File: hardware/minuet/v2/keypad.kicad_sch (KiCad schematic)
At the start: 3 parts, among them J501 G800LE300018YEU, J502 MTJ-889X1, J503 MTJ-669X1

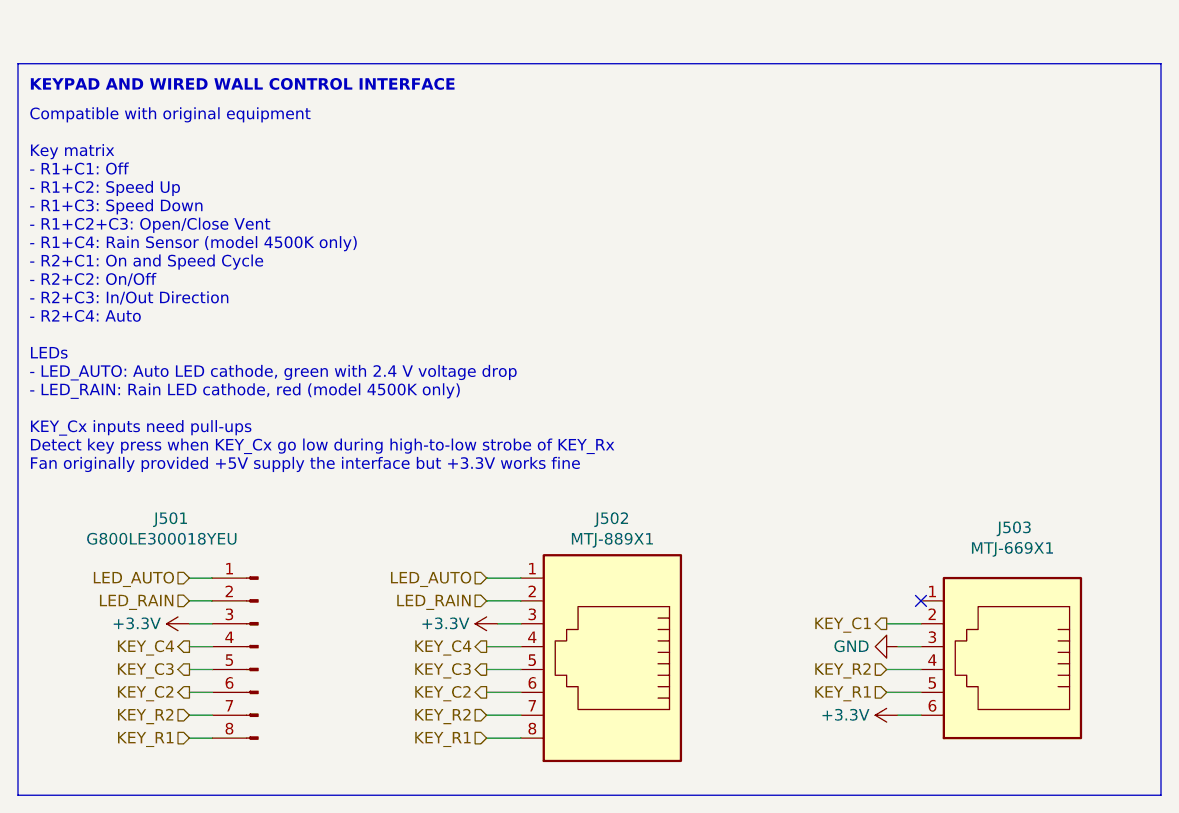
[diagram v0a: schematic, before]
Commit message: Finalize Minuet v2.1 for manufacture.
This revision uses a different motor controller and buck converter
and remedies errata from v2.0.
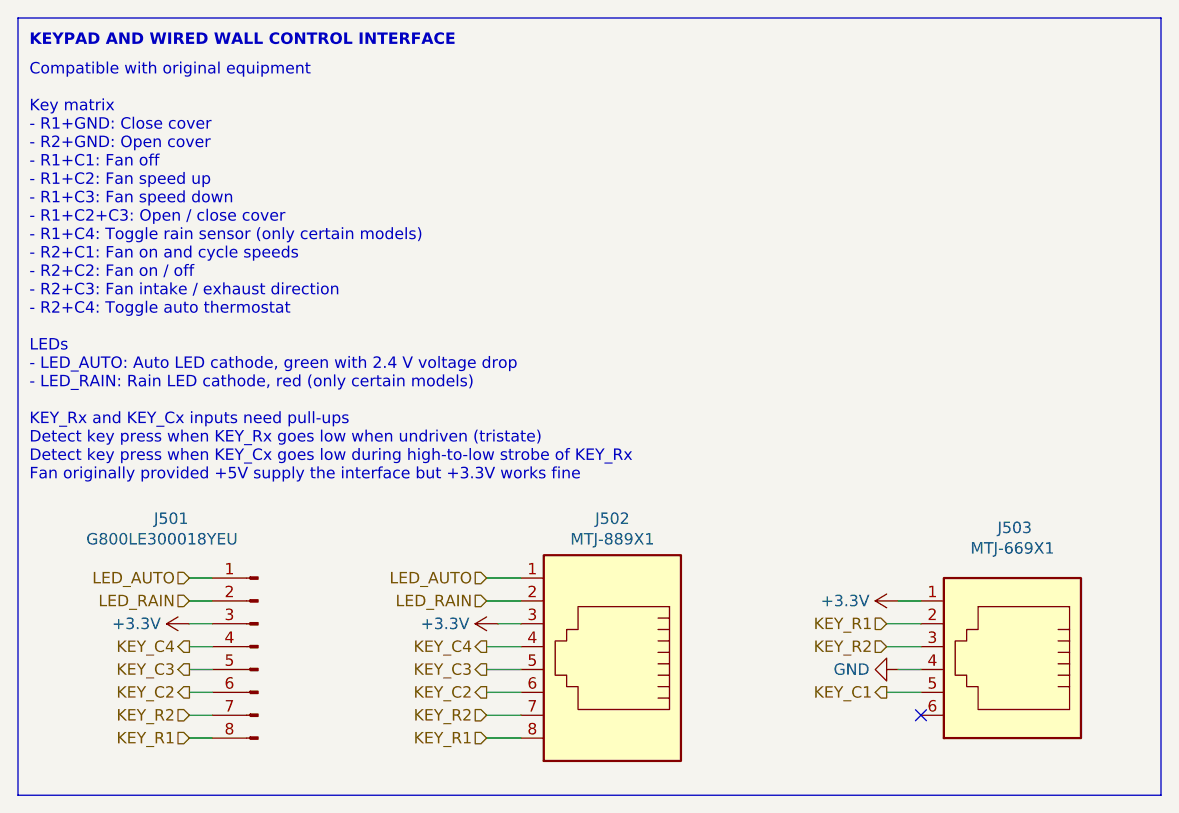
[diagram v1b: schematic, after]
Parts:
- J501: LCSC (none) -> C3345591
- J502: LCSC (none) -> C6105889
- J503: LCSC (none) -> C5785037
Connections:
- net +3.3V: now also J503.1; no longer J503.6
- net GND: now also J503.4; no longer J503.3
- net KEY_C1: now also J503.5; no longer J503.2
- net KEY_R1: now also J503.2; no longer J503.5
- net KEY_R2: now also J503.3; no longer J503.4
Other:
- note added: "Compatible with original equipment Key matrix - R1+GND: Close cover - R2+GND: Open cover - R1+C1: Fan off - R1+C2: Fan speed up - R1+C3: Fan speed down - R1+C2+C3: Open / close cover - R1+C4: Toggle rain sensor (only certain models) - R2+C1: Fan on and cycle speeds - R2+C2: Fan on / off - R2+C3: Fan intake / exhaust direction - R2+C4: Toggle auto thermostat LEDs - LED_AUTO: Auto LED cathode, gree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"
- note removed: "Compatible with original equipment Key matrix - R1+C1: Off - R1+C2: Speed Up - R1+C3: Speed Down - R1+C2+C3: Open/Close Vent - R1+C4: Rain Sensor (model 4500K only) - R2+C1: On and Speed Cycle - R2+C2: On/Off - R2+C3: In/Out Direction - R2+C4: Auto LEDs - LED_AUTO: Auto LED cathode, green with 2.4 V voltage drop - LED_RAIN: Rain LED cathode, red (model 4500K only) KEY_Cx inputs need pull-ups Dete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"
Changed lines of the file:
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@@
 	)
 	(no_connect
-		(at 194.31 119.38)
+		(at 194.31 132.08)
 	)
 	(wire
@@
 	(wire
 		(pts
-			(xy 194.31 124.46) (xy 191.77 124.46)
+			(xy 194.31 127) (xy 191.77 127)
 		)
 		(stroke
@@
 	(wire
 		(pts
+			(xy 194.31 121.92) (xy 190.5 121.92)
+		)
+		(stroke
+			(width 0)
+			(type default)
+		)
+	)
+	(wire
+		(pts
+			(xy 113.03 127) (xy 115.57 127)
+		)
+		(stroke
+			(width 0)
+			(type default)
+		)
+	)
+	(wire
+		(pts
+			(xy 194.31 119.38) (xy 191.77 119.38)
+		)
+		(stroke
+			(width 0)
+			(type default)
+		)
+	)
+	(wire
+		(pts
+			(xy 149.86 124.46) (xy 146.05 124.46)
+		)
+		(stroke
+			(width 0)
+			(type default)
+		)
+	)
+	(wire
+		(pts
+			(xy 149.86 127) (xy 146.05 127)
+		)
+		(stroke
+			(width 0)
+			(type default)
+		)
+	)
+	(wire
+		(pts
+			(xy 194.31 124.46) (xy 190.5 124.46)
+		)
+		(stroke
+			(width 0)
+			(type default)
+		)
+	)
+	(wire
+		(pts
+			(xy 149.86 129.54) (xy 146.05 129.54)
+		)
+		(stroke
+			(width 0)
+			(type default)
+		)
+	)
+	(wire
+		(pts
 			(xy 194.31 129.54) (xy 190.5 129.54)
 		)
@@
 	(wire
 		(pts
-			(xy 113.03 127) (xy 115.57 127)
-		)
-		(stroke
-			(width 0)
-			(type default)
-		)
-	)
-	(wire
-		(pts
-			(xy 194.31 132.08) (xy 191.77 132.08)
-		)
-		(stroke
-			(width 0)
-			(type default)
-		)
-	)
-	(wire
-		(pts
-			(xy 149.86 124.46) (xy 146.05 124.46)
-		)
-		(stroke
-			(width 0)
-			(type default)
-		)
-	)
-	(wire
-		(pts
-			(xy 149.86 127) (xy 146.05 127)
-		)
-		(stroke
-			(width 0)
-			(type default)
-		)
-	)
-	(wire
-		(pts
-			(xy 194.31 127) (xy 190.5 127)
-		)
-		(stroke
-			(width 0)
-			(type default)
-		)
-	)
-	(wire
-		(pts
-			(xy 149.86 129.54) (xy 146.05 129.54)
-		)
-		(stroke
-			(width 0)
-			(type default)
-		)
-	)
-	(wire
-		(pts
-			(xy 194.31 121.92) (xy 190.5 121.92)
-		)
-		(stroke
-			(width 0)
-			(type default)
-		)
-	)
-	(wire
-		(pts
 			(xy 113.03 134.62) (xy 115.57 134.62)
 		)
@@
 	)
 	(rectangle
-		(start 93.98 59.69)
+		(start 93.98 54.61)
 		(end 220.98 140.97)
 		(stroke
@@
 		)
 	)
-	(text "Compatible with original equipment\n\nKey matrix\n- R1+C1: Off\n- R1+C2: Speed Up\n- R1+C3: Speed Down\n- R1+C2+C3: Open/Close Vent\n- R1+C4: Rain Sensor (model 4500K only)\n- R2+C1: On and Speed Cycle\n- R2+C2: On/Off\n- R2+C3: In/Out Direction\n- R2+C4: Auto\n\nLEDs\n- LED_AUTO: Auto LED cathode, green with 2.4 V voltage drop\n- LED_RAIN: Rain LED cathode, red (model 4500K only)\n\nKEY_Cx inputs need pull-ups\nDetect key press when KEY_Cx go low during high-to-low strobe of KEY_Rx\nFan originally provided +5V supply the interface but +3.3V works fine"
+	(text "Compatible with original equipment\n\nKey matrix\n- R1+GND: Close cover\n- R2+GND: Open cover\n- R1+C1: Fan off\n- R1+C2: Fan speed up\n- R1+C3: Fan speed down\n- R1+C2+C3: Open / close cover\n- R1+C4: Toggle rain sensor (only certain models)\n- R2+C1: Fan on and cycle speeds\n- R2+C2: Fan on / off\n- R2+C3: Fan intake / exhaust direction\n- R2+C4: Toggle auto thermostat\n\nLEDs\n- LED_AUTO: Auto LED cathode, green with 2.4 V voltage drop\n- LED_RAIN: Rain LED cathode, red (only certain models)\n\nKEY_Rx and KEY_Cx inputs need pull-ups\nDetect key press when KEY_Rx goes low when undriven (tristate)\nDetect key press when KEY_Cx goes low during high-to-low strobe of KEY_Rx\nFan originally provided +5V supply the interface but +3.3V works fine"
 		(exclude_from_sim no)
-		(at 95.25 64.77 0)
+		(at 95.25 59.69 0)
 		(effects
 			(font
@@
 	(text "KEYPAD AND WIRED WALL CONTROL INTERFACE"
 		(exclude_from_sim no)
-		(at 95.25 62.23 0)
+		(at 95.25 57.15 0)
 		(effects
 			(font
@@
 	(hierarchical_label "KEY_R2"
 		(shape input)
-		(at 190.5 127 180)
+		(at 190.5 124.46 180)
 		(effects
 			(font
@@
 	(hierarchical_label "KEY_C1"
 		(shape output)
-		(at 190.5 121.92 180)
+		(at 190.5 129.54 180)
 		(effects
 			(font
@@
 	(hierarchical_label "KEY_R1"
 		(shape input)
-		(at 190.5 129.54 180)
+		(at 190.5 121.92 180)
 		(effects
 			(font
@@
 		(dnp no)
 		(fields_autoplaced yes)
-		(property "Reference" "#PWR0501"
+		(property "Reference" "#PWR0502"
 			(at 116.84 121.92 0)
 			(effects
@@
 			(project "minuet"
 				(path "/5bd7983a-3caa-4bb2-9dc5-1af533f31e50/ecd3cea2-5b83-45e6-bc3a-38348e0ff880"
-					(reference "#PWR0501")
+					(reference "#PWR0502")
 					(unit 1)
 				)
@@
 			)
 		)
+		(property "LCSC" "C5785037"
+			(at 204.47 124.46 0)
+			(effects
+				(font
+					(size 1.27 1.27)
+				)
+				(hide yes)
+			)
+		)
 		(pin "2"
 		)
@@
 			)
 		)
+		(property "LCSC" "C6105889"
+			(at 160.02 124.46 0)
+			(effects
+				(font
+					(size 1.27 1.27)
+				)
+				(hide yes)
+			)
+		)
 		(pin "2"
 		)
@@
 		(dnp no)
 		(fields_autoplaced yes)
-		(property "Reference" "#PWR0502"
+		(property "Reference" "#PWR0503"
 			(at 151.13 121.92 0)
 			(effects
@@
 		(property "Description" "Power symbol creates a global label with name \"+3.3V\""
 			(at 147.32 121.92 0)
-			(effects
-				(font
-					(size 1.27 1.27)
-				)
-				(hide yes)
-			)
-		)
-		(pin "1"
-		)
-		(instances
-			(project "minuet"
-				(path "/5bd7983a-3caa-4bb2-9dc5-1af533f31e50/ecd3cea2-5b83-45e6-bc3a-38348e0ff880"
-					(reference "#PWR0502")
-					(unit 1)
-				)
-			)
-		)
-	)
-	(symbol
-		(lib_id "power:GND")
-		(at 191.77 124.46 270)
-		(unit 1)
-		(exclude_from_sim no)
-		(in_bom yes)
-		(on_board yes)
-		(dnp no)
-		(fields_autoplaced yes)
-		(property "Reference" "#PWR0503"
-			(at 185.42 124.46 0)
-			(effects
-				(font
-					(size 1.27 1.27)
-				)
-				(hide yes)
-			)
-		)
-		(property "Value" "GND"
-			(at 188.595 124.46 90)
-			(effects
-				(font
-					(size 1.27 1.27)
-				)
-				(justify right)
-			)
-		)
-		(property "Footprint" ""
-			(at 191.77 124.46 0)
-			(effects
-				(font
-					(size 1.27 1.27)
-				)
-				(hide yes)
-			)
-		)
-		(property "Datasheet" ""
-			(at 191.77 124.46 0)
-			(effects
-				(font
-					(size 1.27 1.27)
-				)
-				(hide yes)
-			)
-		)
-		(property "Description" "Power symbol creates a global label with name \"GND\" , ground"
-			(at 191.77 124.46 0)
 			(effects
 				(font
@@
 	)
 	(symbol
-		(lib_id "power:+3.3V")
-		(at 191.77 132.08 90)
+		(lib_id "power:GND")
+		(at 191.77 127 270)
+		(mirror x)
 		(unit 1)
 		(exclude_from_sim no)
@@
 		(fields_autoplaced yes)
 		(property "Reference" "#PWR0504"
-			(at 195.58 132.08 0)
-			(effects
-				(font
-					(size 1.27 1.27)
-				)
-				(hide yes)
-			)
-		)
-		(property "Value" "+3.3V"
-			(at 188.595 132.08 90)
-			(effects
-				(font
-					(size 1.27 1.27)
-				)
-				(justify left)
+			(at 185.42 127 0)
+			(effects
+				(font
+					(size 1.27 1.27)
+				)
+				(hide yes)
+			)
+		)
+		(property "Value" "GND"
+			(at 188.595 127 90)
+			(effects
+				(font
+					(size 1.27 1.27)
+				)
+				(justify right)
 			)
 		)
 		(property "Footprint" ""
-			(at 191.77 132.08 0)
+			(at 191.77 127 0)
 			(effects
 				(font
@@
 		)
 		(property "Datasheet" ""
-			(at 191.77 132.08 0)
-			(effects
-				(font
-					(size 1.27 1.27)
-				)
-				(hide yes)
-			)
-		)
-		(property "Description" "Power symbol creates a global label with name \"+3.3V\""
-			(at 191.77 132.08 0)
+			(at 191.77 127 0)
+			(effects
+				(font
+					(size 1.27 1.27)
+				)
+				(hide yes)
+			)
+		)
+		(property "Description" "Power symbol creates a global label with name \"GND\" , ground"
+			(at 191.77 127 0)
 			(effects
 				(font
@@
 				(path "/5bd7983a-3caa-4bb2-9dc5-1af533f31e50/ecd3cea2-5b83-45e6-bc3a-38348e0ff880"
 					(reference "#PWR0504")
+					(unit 1)
+				)
+			)
+		)
+	)
+	(symbol
+		(lib_id "power:+3.3V")
+		(at 191.77 119.38 90)
+		(mirror x)
+		(unit 1)
+		(exclude_from_sim no)
+		(in_bom yes)
+		(on_board yes)
+		(dnp no)
+		(fields_autoplaced yes)
+		(property "Reference" "#PWR0501"
+			(at 195.58 119.38 0)
+			(effects
+				(font
+					(size 1.27 1.27)
+				)
+				(hide yes)
+			)
+		)
+		(property "Value" "+3.3V"
+			(at 188.595 119.38 90)
+			(effects
+				(font
+					(size 1.27 1.27)
+				)
+				(justify left)
+			)
+		)
+		(property "Footprint" ""
+			(at 191.77 119.38 0)
+			(effects
+				(font
+					(size 1.27 1.27)
+				)
+				(hide yes)
+			)
+		)
+		(property "Datasheet" ""
+			(at 191.77 119.38 0)
+			(effects
+				(font
+					(size 1.27 1.27)
+				)
+				(hide yes)
+			)
+		)
+		(property "Description" "Power symbol creates a global label with name \"+3.3V\""
+			(at 191.77 119.38 0)
+			(effects
+				(font
+					(size 1.27 1.27)
+				)
+				(hide yes)
+			)
+		)
+		(pin "1"
+		)
+		(instances
+			(project "minuet"
+				(path "/5bd7983a-3caa-4bb2-9dc5-1af533f31e50/ecd3cea2-5b83-45e6-bc3a-38348e0ff880"
+					(reference "#PWR0501")
 					(unit 1)
 				)
@@
 			(at 120.65 124.46 0)
 			(effects
+				(font
+					(size 1.27 1.27)
+				)
+				(hide yes)
+			)
+		)
+		(property "LCSC" "C3345591"
+			(at 120.65 124.46 0)
+			(effects
